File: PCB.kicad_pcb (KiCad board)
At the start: 4 copper layers, 200 x 150 mm, 517 parts, among them J1 PASSIVE_CHANNELS, J10 USB_RASPBERRY, J11 USB_ARDUINO, J12 100W_ch+, J13 100W_ch-, J14 100W_sense, J15 PowerMosGate, J16 PowerMosDrain, J2 PASSIVE_CHANNELS, J3 PASSIVE_CHANNELS, J4 12V+, J5 12V-, J6 5V_PI, J7 5V_PI, J8 ACTIVE_5W_CHANNELS, J9 5V_PI, Q1 BT137-600, Q10 IRLB3813PBF, Q11 IRLB3813PBF, Q12 IRLB3813PbF, Q13 IRLB3813PbF, Q14 IRLB3813PbF, Q15 IRLB3813PbF, Q16 IRLB3813PbF, Q17 IRLB3813PbF, Q2 IRLB3813PbF, Q3 IRLB3813PbF, Q4 IRLB3813PBF, Q5 IRLB3813PBF, Q6 IRLB3813PBF, Q7 IRLB3813PBF, Q8 IRLB3813PBF, Q9 IRLB3813PBF, SW1 RESET_SW, T1+1 TestPoint, T1+2 TestPoint, T1+3 TestPoint, T1+4 TestPoint, T1+5 TestPoint, T1+6 TestPoint, T1+7 TestPoint, T1+8 TestPoint, T1-1 TestPoint, T1-2 TestPoint, T1-3 TestPoint, T1-4 TestPoint, T1-5 TestPoint, T1-6 TestPoint, T1-7 TestPoint, T1-8 TestPoint, T2+1 TestPoint, T2+2 TestPoint, T2+3 TestPoint, T2+4 TestPoint, T2+5 TestPoint, T2+6 TestPoint, T2+7 TestPoint, T2+8 TestPoint, T2-1 TestPoint, T2-2 TestPoint, T2-3 TestPoint, T2-4 TestPoint, T2-5 TestPoint, T2-6 TestPoint, T2-7 TestPoint, T2-8 TestPoint, U1 LM431ACM3_NOPB, U10 INA250A4PW, U11 INA250A4PW, U12 INA250A4PW, U13 ADC124S021CIMM_NOPB, U14 INA250A4PW, U15 INA250A4PW, U16 INA250A4PW, U17 INA250A4PW, U18 ADC124S021CIMM_NOPB, U19 INA250A4PW, U2 LM1117-ADJ, U20 INA250A4PW, U21 INA250A4PW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

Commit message: Placement charge active fini
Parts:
- moved R84 85.3 mm to (280.2, 158.0), turned to 180 degrees
- moved R83 82.3 mm to (283.2, 158.0), turned to 180 degrees
- moved TPV-1 82.2 mm to (297.6, 183.7), turned to 270 degrees
- moved R127 78.3 mm to (297.3, 181.8), turned to 180 degrees
- moved U29 77.4 mm to (282.2, 153.5), turned to 270 degrees
- moved C101 76.4 mm to (297.6, 179.9), turned to 0 degrees
- moved R131 74.4 mm to (300.8, 181.8), turned to 0 degrees
- moved R86 72.8 mm to (280.5, 149.0), turned to 180 degrees
- moved R133 72.8 mm to (300.8, 180.1), turned to 180 degrees
- moved J13 72.6 mm to (310.2, 186.2), turned to 0 degrees
- moved U36 70.4 mm to (299.4, 175.4), turned to 270 degrees
- moved R85 69.5 mm to (283.5, 149.0), turned to 180 degrees
- moved R129 69.2 mm to (297.7, 170.7), turned to 180 degrees
- moved C103 68.2 mm to (297.7, 169.2), turned to 0 degrees
- moved R128 67.7 mm to (296.8, 166.9), turned to 270 degrees
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
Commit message: Petit ajustement pour accomoder le usb du arduino, pret pour routing
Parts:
- moved TPVA7 273.8 mm to (317.0, 84.0)
- moved TPVA6 271.6 mm to (305.8, 77.0)
- moved TPVS+1 225.5 mm to (307.8, 137.0), turned to 90 degrees
- moved TPVA2 224.9 mm to (250.8, 77.0)
- moved TPVA1 218.0 mm to (239.8, 77.0)
- moved TPVS-1 210.4 mm to (296.8, 143.8), turned to 90 degrees
- moved TPVA5 206.6 mm to (294.8, 77.0)
- moved TPVA4 195.6 mm to (283.8, 77.0)
- moved TPVA3 184.6 mm to (272.8, 77.0)
- moved TPVA8 173.7 mm to (261.8, 77.0)
- moved TPVP8 170.0 mm to (221.8, 84.5)
- moved TPVP7 169.9 mm to (212.8, 77.0)
- moved TPVP6 164.4 mm to (201.8, 77.0)
- moved TPVP5 158.6 mm to (190.8, 77.0)
- moved TPVP4 152.9 mm to (179.8, 77.0)
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- renumbered TPOA1 to OA1, TPOB1 to OB1, TPVA4 to TPVA3, TPVA5 to TPVA4, TPVA6 to TPVA5, TPVA7 to TPVA6, TPVA8 to TPVA7, TPVA3 to TPVA8, TPV+1 to V+3, V+3 to V+4, V+4 to V+5, V+5 to V+6, V+6 to V+7, V+7 to V+8, V+8 to V+9, TPV-1 to V-3, V-3 to V-4, V-4 to V-5, V-5 to V-6, V-6 to V-7, V-7 to V-8, V-8 to V-9, TPVAD1 to VAD3, VAD3 to VAD4, VAD4 to VAD5, VAD5 to VAD6, VAD6 to VAD7, VAD7 to VAD8, VAD8 to VAD9, TPVGS1 to VGS3, VGS3 to VGS4, VGS4 to VGS5, VGS5 to VGS6, VGS6 to VGS7, VGS7 to VGS8, VGS8 to VGS9
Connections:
- J10 pad 1: (no net) -> Net-(J10-Pad1)
- J11 pad 1: (no net) -> Net-(J11-Pad1)
- S2 pad 1: (no net) -> Net-(S2-Pad1)
- S3 pad 1: (no net) -> Net-(S3-Pad1)
- S4 pad 1: (no net) -> Net-(S4-Pad1)
- S5 pad 1: (no net) -> Net-(S5-Pad1)
- S6 pad 1: (no net) -> Net-(S6-Pad1)
- TPVA8 pad 1: /sheet6116B43F/Input -> Net-(TPVA8-Pad1)
- XA1 pad 3V3: (no net) -> Net-(XA1-Pad3V3)
- XA1 pad 5V2: (no net) -> Net-(XA1-Pad5V2)
- XA1 pad AREF: (no net) -> Net-(XA1-PadAREF)
- XA1 pad D0: (no net) -> Net-(XA1-PadD0)
- XA1 pad D1: (no net) -> Net-(XA1-PadD1)
- XA1 pad D12: (no net) -> Net-(XA1-PadD12)
- XA1 pad D13: (no net) -> Net-(XA1-PadD13)
- XA1 pad D14: (no net) -> Net-(XA1-PadD14)
- XA1 pad D15: (no net) -> Net-(XA1-PadD15)
- XA1 pad D16: (no net) -> Net-(XA1-PadD16)
- XA1 pad D17: (no net) -> Net-(XA1-PadD17)
- XA1 pad D18: (no net) -> Net-(XA1-PadD18)
- XA1 pad D19: (no net) -> Net-(XA1-PadD19)
- XA1 pad D20: (no net) -> Net-(XA1-PadD20)
- XA1 pad D21: (no net) -> Net-(XA1-PadD21)
- XA1 pad D35: (no net) -> Net-(XA1-PadD35)
- XA1 pad D36: (no net) -> Net-(XA1-PadD36)
- XA1 pad D37: (no net) -> Net-(XA1-PadD37)
- XA1 pad D38: (no net) -> Net-(XA1-PadD38)
- XA1 pad D39: (no net) -> Net-(XA1-PadD39)
- XA1 pad D4: (no net) -> Net-(XA1-PadD4)
- XA1 pad D40: (no net) -> Net-(XA1-PadD40)
- XA1 pad D41: (no net) -> Net-(XA1-PadD41)
- XA1 pad D42: (no net) -> Net-(XA1-PadD42)
- XA1 pad D43: (no net) -> Net-(XA1-PadD43)
- XA1 pad D44: (no net) -> Net-(XA1-PadD44)
- XA1 pad D45: (no net) -> Net-(XA1-PadD45)
- XA1 pad GND4: (no net) -> Net-(XA1-PadGND4)
- XA1 pad IORF: (no net) -> Net-(XA1-PadIORF)
- XA1 pad RST2: (no net) -> Net-(XA1-PadRST2)
- XA1 pad SCL: (no net) -> Net-(XA1-PadSCL)
- XA1 pad SDA: (no net) -> Net-(XA1-PadSDA)
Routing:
- net /SenseProtection-/Input: track 0.00 -> 1.84 mm

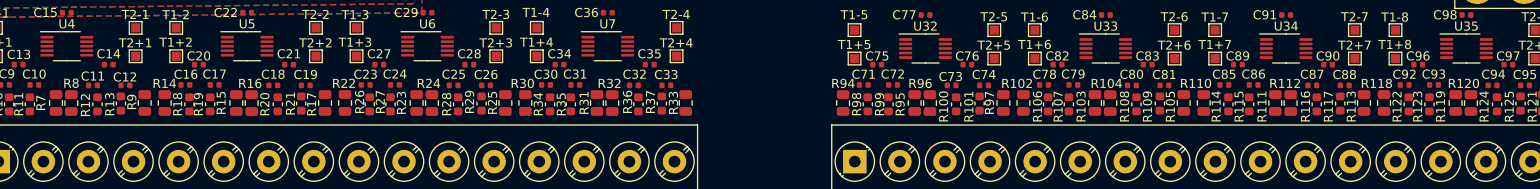
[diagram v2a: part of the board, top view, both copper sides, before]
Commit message: Ajustement resistors température pour routing
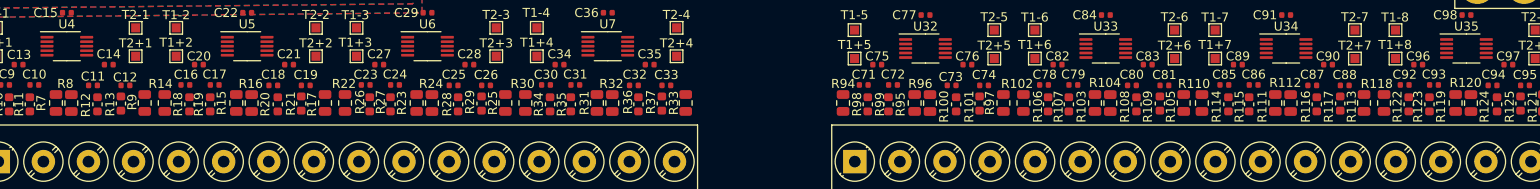
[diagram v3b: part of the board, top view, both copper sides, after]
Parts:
- moved R110 0.20 mm to (274.5, 203.0)
- turned R104 to 270 degrees
- turned R112 to 270 degrees
- turned R120 to 270 degrees
- turned R16 to 270 degrees
- turned R24 to 270 degrees
- turned R32 to 270 degrees
- turned R8 to 270 degrees
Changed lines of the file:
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@@
   )
   (module Resistor_SMD:R_0805_2012Metric (layer F.Cu)
-    (at 149.1 203.0085 90)
+    (at 149.1 203.0085 270)
     (descr "Resistor SMD 0805 (2012 Metric), square (rectangular) end terminal, IPC_7351 nominal, (Body size source: https://docs.google.com/spreadsheets/d/1BsfQQcO9C6DZCsRaXUlFlo91Tg2WpOkGARC1WS5S8t0/edit?usp=sharing), generated with kicad-footprint-generator")
     (tags resistor)
     (attr smd)
-    (fp_text reference R8 (at 2.1625 0 180) (layer F.SilkS)
+    (fp_text reference R8 (at -2.1465 0.662 180) (layer F.SilkS)
       (effects (font (size 1 1) (thickness 0.15)))
     )
@@
     (fp_line (start -1 -0.6) (end 1 -0.6) (layer F.Fab) (width 0.1))
     (fp_line (start -1 0.6) (end -1 -0.6) (layer F.Fab) (width 0.1))
-    (pad 2 smd roundrect (at 0.9375 0 90) (size 0.975 1.4) (layers F.Cu F.Paste F.Mask) (roundrect_rratio 0.25)
+    (pad 2 smd roundrect (at 0.9375 0 270) (size 0.975 1.4) (layers F.Cu F.Paste F.Mask) (roundrect_rratio 0.25)
       (net 104 /T2+))
-    (pad 1 smd roundrect (at -0.9375 0 90) (size 0.975 1.4) (layers F.Cu F.Paste F.Mask) (roundrect_rratio 0.25)
+    (pad 1 smd roundrect (at -0.9375 0 270) (size 0.975 1.4) (layers F.Cu F.Paste F.Mask) (roundrect_rratio 0.25)
       (net 11 /+5V))
     (model ${KISYS3DMOD}/Resistor_SMD.3dshapes/R_0805_2012Metric.wrl
@@
     (tags resistor)
     (attr smd)
-    (fp_text reference R14 (at -2.134 0.024) (layer F.SilkS)
+    (fp_text reference R14 (at -2.134 0.462) (layer F.SilkS)
       (effects (font (size 1 1) (thickness 0.15)))
     )
@@
   )
   (module Resistor_SMD:R_0805_2012Metric (layer F.Cu)
-    (at 169.1 203.0085 90)
+    (at 169.1 203.0085 270)
     (descr "Resistor SMD 0805 (2012 Metric), square (rectangular) end terminal, IPC_7351 nominal, (Body size source: https://docs.google.com/spreadsheets/d/1BsfQQcO9C6DZCsRaXUlFlo91Tg2WpOkGARC1WS5S8t0/edit?usp=sharing), generated with kicad-footprint-generator")
     (tags resistor)
     (attr smd)
-    (fp_text reference R16 (at 2.1465 -0.174 180) (layer F.SilkS)
+    (fp_text reference R16 (at -2.1465 0.1 180) (layer F.SilkS)
       (effects (font (size 1 1) (thickness 0.15)))
     )
@@
     (fp_line (start -1 -0.6) (end 1 -0.6) (layer F.Fab) (width 0.1))
     (fp_line (start -1 0.6) (end -1 -0.6) (layer F.Fab) (width 0.1))
-    (pad 2 smd roundrect (at 0.9375 0 90) (size 0.975 1.4) (layers F.Cu F.Paste F.Mask) (roundrect_rratio 0.25)
+    (pad 2 smd roundrect (at 0.9375 0 270) (size 0.975 1.4) (layers F.Cu F.Paste F.Mask) (roundrect_rratio 0.25)
       (net 108 /T4+))
-    (pad 1 smd roundrect (at -0.9375 0 90) (size 0.975 1.4) (layers F.Cu F.Paste F.Mask) (roundrect_rratio 0.25)
+    (pad 1 smd roundrect (at -0.9375 0 270) (size 0.975 1.4) (layers F.Cu F.Paste F.Mask) (roundrect_rratio 0.25)
       (net 11 /+5V))
     (model ${KISYS3DMOD}/Resistor_SMD.3dshapes/R_0805_2012Metric.wrl
@@
   )
   (module Resistor_SMD:R_0805_2012Metric (layer F.Cu)
-    (at 189.1 203.0085 90)
+    (at 189.1 203.0085 270)
     (descr "Resistor SMD 0805 (2012 Metric), square (rectangular) end terminal, IPC_7351 nominal, (Body size source: https://docs.google.com/spreadsheets/d/1BsfQQcO9C6DZCsRaXUlFlo91Tg2WpOkGARC1WS5S8t0/edit?usp=sharing), generated with kicad-footprint-generator")
     (tags resistor)
     (attr smd)
-    (fp_text reference R24 (at 2.1465 -0.362 180) (layer F.SilkS)
+    (fp_text reference R24 (at -2.1465 0.1 180) (layer F.SilkS)
       (effects (font (size 1 1) (thickness 0.15)))
     )
@@
       (effects (font (size 0.5 0.5) (thickness 0.08)))
     )
-    (pad 1 smd roundrect (at -0.9375 0 90) (size 0.975 1.4) (layers F.Cu F.Paste F.Mask) (roundrect_rratio 0.25)
+    (pad 1 smd roundrect (at -0.9375 0 270) (size 0.975 1.4) (layers F.Cu F.Paste F.Mask) (roundrect_rratio 0.25)
       (net 11 /+5V))
-    (pad 2 smd roundrect (at 0.9375 0 90) (size 0.975 1.4) (layers F.Cu F.Paste F.Mask) (roundrect_rratio 0.25)
+    (pad 2 smd roundrect (at 0.9375 0 270) (size 0.975 1.4) (layers F.Cu F.Paste F.Mask) (roundrect_rratio 0.25)
       (net 112 /T6+))
     (model ${KISYS3DMOD}/Resistor_SMD.3dshapes/R_0805_2012Metric.wrl
@@
   )
   (module Resistor_SMD:R_0805_2012Metric (layer F.Cu)
-    (at 209.1 203.0085 90)
+    (at 209.1 203.0085 270)
     (descr "Resistor SMD 0805 (2012 Metric), square (rectangular) end terminal, IPC_7351 nominal, (Body size source: https://docs.google.com/spreadsheets/d/1BsfQQcO9C6DZCsRaXUlFlo91Tg2WpOkGARC1WS5S8t0/edit?usp=sharing), generated with kicad-footprint-generator")
     (tags resistor)
     (attr smd)
-    (fp_text reference R32 (at 2.1465 -0.296 180) (layer F.SilkS)
+    (fp_text reference R32 (at -2.1465 0.1 180) (layer F.SilkS)
       (effects (font (size 1 1) (thickness 0.15)))
     )
@@
     (fp_line (start -1 -0.6) (end 1 -0.6) (layer F.Fab) (width 0.1))
     (fp_line (start -1 0.6) (end -1 -0.6) (layer F.Fab) (width 0.1))
-    (pad 2 smd roundrect (at 0.9375 0 90) (size 0.975 1.4) (layers F.Cu F.Paste F.Mask) (roundrect_rratio 0.25)
+    (pad 2 smd roundrect (at 0.9375 0 270) (size 0.975 1.4) (layers F.Cu F.Paste F.Mask) (roundrect_rratio 0.25)
       (net 116 /T8+))
-    (pad 1 smd roundrect (at -0.9375 0 90) (size 0.975 1.4) (layers F.Cu F.Paste F.Mask) (roundrect_rratio 0.25)
+    (pad 1 smd roundrect (at -0.9375 0 270) (size 0.975 1.4) (layers F.Cu F.Paste F.Mask) (roundrect_rratio 0.25)
       (net 11 /+5V))
     (model ${KISYS3DMOD}/Resistor_SMD.3dshapes/R_0805_2012Metric.wrl
@@
   )
   (module Resistor_SMD:R_0805_2012Metric (layer F.Cu)
-    (at 264.34 203.0085 90)
+    (at 264.34 203.0085 270)
     (descr "Resistor SMD 0805 (2012 Metric), square (rectangular) end terminal, IPC_7351 nominal, (Body size source: https://docs.google.com/spreadsheets/d/1BsfQQcO9C6DZCsRaXUlFlo91Tg2WpOkGARC1WS5S8t0/edit?usp=sharing), generated with kicad-footprint-generator")
     (tags resistor)
     (attr smd)
-    (fp_text reference R104 (at 2.1465 -0.418) (layer F.SilkS)
+    (fp_text reference R104 (at -2.2585 0.59) (layer F.SilkS)
       (effects (font (size 1 1) (thickness 0.15)))
     )
@@
       (effects (font (size 0.5 0.5) (thickness 0.08)))
     )
-    (pad 1 smd roundrect (at -0.9375 0 90) (size 0.975 1.4) (layers F.Cu F.Paste F.Mask) (roundrect_rratio 0.25)
+    (pad 1 smd roundrect (at -0.9375 0 270) (size 0.975 1.4) (layers F.Cu F.Paste F.Mask) (roundrect_rratio 0.25)
       (net 11 /+5V))
-    (pad 2 smd roundrect (at 0.9375 0 90) (size 0.975 1.4) (layers F.Cu F.Paste F.Mask) (roundrect_rratio 0.25)
+    (pad 2 smd roundrect (at 0.9375 0 270) (size 0.975 1.4) (layers F.Cu F.Paste F.Mask) (roundrect_rratio 0.25)
       (net 95 /T12+))
     (model ${KISYS3DMOD}/Resistor_SMD.3dshapes/R_0805_2012Metric.wrl
@@
   )
   (module Resistor_SMD:R_0805_2012Metric (layer F.Cu)
-    (at 274.702 202.996 270)
+    (at 274.5 203 270)
     (descr "Resistor SMD 0805 (2012 Metric), square (rectangular) end terminal, IPC_7351 nominal, (Body size source: https://docs.google.com/spreadsheets/d/1BsfQQcO9C6DZCsRaXUlFlo91Tg2WpOkGARC1WS5S8t0/edit?usp=sharing), generated with kicad-footprint-generator")
     (tags resistor)
@@
   )
   (module Resistor_SMD:R_0805_2012Metric (layer F.Cu)
-    (at 284.34 203.0085 90)
+    (at 284.34 203.0085 270)
     (descr "Resistor SMD 0805 (2012 Metric), square (rectangular) end terminal, IPC_7351 nominal, (Body size source: https://docs.google.com/spreadsheets/d/1BsfQQcO9C6DZCsRaXUlFlo91Tg2WpOkGARC1WS5S8t0/edit?usp=sharing), generated with kicad-footprint-generator")
     (tags resistor)
     (attr smd)
-    (fp_text reference R112 (at 2.1465 -0.606 180) (layer F.SilkS)
+    (fp_text reference R112 (at -2.2585 0.59 180) (layer F.SilkS)
       (effects (font (size 1 1) (thickness 0.15)))
     )
@@
     (fp_line (start -1 -0.6) (end 1 -0.6) (layer F.Fab) (width 0.1))
     (fp_line (start -1 0.6) (end -1 -0.6) (layer F.Fab) (width 0.1))
-    (pad 2 smd roundrect (at 0.9375 0 90) (size 0.975 1.4) (layers F.Cu F.Paste F.Mask) (roundrect_rratio 0.25)
+    (pad 2 smd roundrect (at 0.9375 0 270) (size 0.975 1.4) (layers F.Cu F.Paste F.Mask) (roundrect_rratio 0.25)
       (net 91 /T14+))
-    (pad 1 smd roundrect (at -0.9375 0 90) (size 0.975 1.4) (layers F.Cu F.Paste F.Mask) (roundrect_rratio 0.25)
+    (pad 1 smd roundrect (at -0.9375 0 270) (size 0.975 1.4) (layers F.Cu F.Paste F.Mask) (roundrect_rratio 0.25)
       (net 11 /+5V))
     (model ${KISYS3DMOD}/Resistor_SMD.3dshapes/R_0805_2012Metric.wrl
@@
   )
   (module Resistor_SMD:R_0805_2012Metric (layer F.Cu)
-    (at 304.34 203.0085 90)
+    (at 304.34 203.0085 270)
     (descr "Resistor SMD 0805 (2012 Metric), square (rectangular) end terminal, IPC_7351 nominal, (Body size source: https://docs.google.com/spreadsheets/d/1BsfQQcO9C6DZCsRaXUlFlo91Tg2WpOkGARC1WS5S8t0/edit?usp=sharing), generated with kicad-footprint-generator")
     (tags resistor)
     (attr smd)
-    (fp_text reference R120 (at 2.1465 -0.794 180) (layer F.SilkS)
+    (fp_text reference R120 (at -2.2585 0.59 180) (layer F.SilkS)
       (effects (font (size 1 1) (thickness 0.15)))
     )
@@
     (fp_line (start -1 -0.6) (end 1 -0.6) (layer F.Fab) (width 0.1))
     (fp_line (start -1 0.6) (end -1 -0.6) (layer F.Fab) (width 0.1))
-    (pad 2 smd roundrect (at 0.9375 0 90) (size 0.975 1.4) (layers F.Cu F.Paste F.Mask) (roundrect_rratio 0.25)
+    (pad 2 smd roundrect (at 0.9375 0 270) (size 0.975 1.4) (layers F.Cu F.Paste F.Mask) (roundrect_rratio 0.25)
       (net 87 /T16+))
-    (pad 1 smd roundrect (at -0.9375 0 90) (size 0.975 1.4) (layers F.Cu F.Paste F.Mask) (roundrect_rratio 0.25)
+    (pad 1 smd roundrect (at -0.9375 0 270) (size 0.975 1.4) (layers F.Cu F.Paste F.Mask) (roundrect_rratio 0.25)
       (net 11 /+5V))
     (model ${KISYS3DMOD}/Resistor_SMD.3dshapes/R_0805_2012Metric.wrl
